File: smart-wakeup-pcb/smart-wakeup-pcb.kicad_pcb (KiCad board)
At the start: 2 copper layers, 42.5 x 29 mm, 21 parts, among them J1 Conn_01x03, J2 Conn_01x02, J3 Conn_01x04, J4 Conn_01x04, J5 Conn_01x02, J6 Conn_01x02, Q1 BSS138, Q2 BSS138, U1 XIAO-ESP32-S3-SMD, U2 MAX98357A

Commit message: reroute
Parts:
- added C4: 0.1u, Capacitor_SMD:C_0603_1608Metric, F.Cu at (143.5, 80.8)
- added U3: TMP102xxDRL, Package_TO_SOT_SMD:SOT-563, F.Cu at (141.0, 81.0)
- R1, R2, R3, R4: value R -> 10k; footprint Capacitor_SMD:C_0603_1608Metric -> Resistor_SMD:R_0603_1608Metric
- moved C1 6.69 mm to (140.2, 93.8), turned to -90 degrees
- moved R5 5.51 mm to (135.0, 92.5), turned to 90 degrees
- moved C2 3.45 mm to (137.7, 92.8), turned to 180 degrees
- moved R6 3.22 mm to (135.0, 89.4), turned to 90 degrees
- moved U2 2.65 mm to (138.4, 89.8), turned to 0 degrees
- moved R2 0.20 mm to (143.5, 84.3)
- moved R1 0.15 mm to (147.0, 81.8)
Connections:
- U1 pad 10: /I2S_BCLK -> /I2C_SCL_3V3
- U1 pad 11: /I2S_DIN -> /SW_1_IN
- U1 pad 3: unconnected-(U1-PA10_A2_D2-Pad3) -> /I2S_LRCLK
- U1 pad 5: /I2C_SDA_3V3 -> /I2S_BCLK
- U1 pad 6: /I2C_SCL_3V3 -> /I2S_DIN
- U1 pad 7: /SW_1_IN -> unconnected-(U1-PB08_A6_D6_TX-Pad7)
- U1 pad 9: /I2S_LRCLK -> /I2C_SDA_3V3
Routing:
- net /SW_1_IN: track 0.00 -> 38.9 mm
- net /I2S_LRCLK: track 3.87 -> 26.5 mm
- net /I2S_BCLK: track 1.91 -> 20.8 mm
- net GND: track 0.00 -> 17.7 mm, vias 0 -> 39
- net +3.3V: track 47.9 -> 65.4 mm
- net +5V: track 85.9 -> 102.6 mm
- net /SW_2_IN: track 0.00 -> 16.3 mm
- net /I2S_DIN: track 6.36 -> 14.9 mm
- net /I2C_SDA_3V3: track 32.9 -> 24.9 mm
- net Net-(J2-Pin_2): track 4.09 -> 10.1 mm, vias 0 -> 1
- net Net-(J2-Pin_1): track 3.75 -> 9.51 mm, vias 0 -> 1
- net /I2C_SCL_3V3: track 33.1 -> 32.2 mm, vias 0 -> 2
- net Net-(U2-GAIN_SLOT): track 3.05 -> 3.81 mm
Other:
- board size 42.5 x 29 mm -> 42.5 x 31.2 mm

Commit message: drc, holes, lux sensor
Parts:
- added C5: 1u, Capacitor_SMD:C_0603_1608Metric, F.Cu at (136.3, 79.0)
- added H1: MountingHole, MountingHole:MountingHole_2.2mm_M2, F.Cu at (112.0, 102.2)
- added H2: MountingHole, MountingHole:MountingHole_2.2mm_M2, F.Cu at (131.3, 77.8)
- added U4: LTR-303ALS-01, OptoDevice:Lite-On_LTR-303ALS-01, F.Cu at (136.3, 81.1)
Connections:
- U1 pad 14: +5V -> unconnected-(U1-5V-Pad14)
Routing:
- net +5V: track 102.6 -> 55.4 mm
- net +3.3V: track 65.4 -> 75.7 mm
- net /I2C_SDA_3V3: track 24.9 -> 29.7 mm
- net GND: track 17.7 -> 21.6 mm, vias 39 -> 41
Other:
- board size 42.5 x 31.2 mm -> 46.2 x 33.2 mm

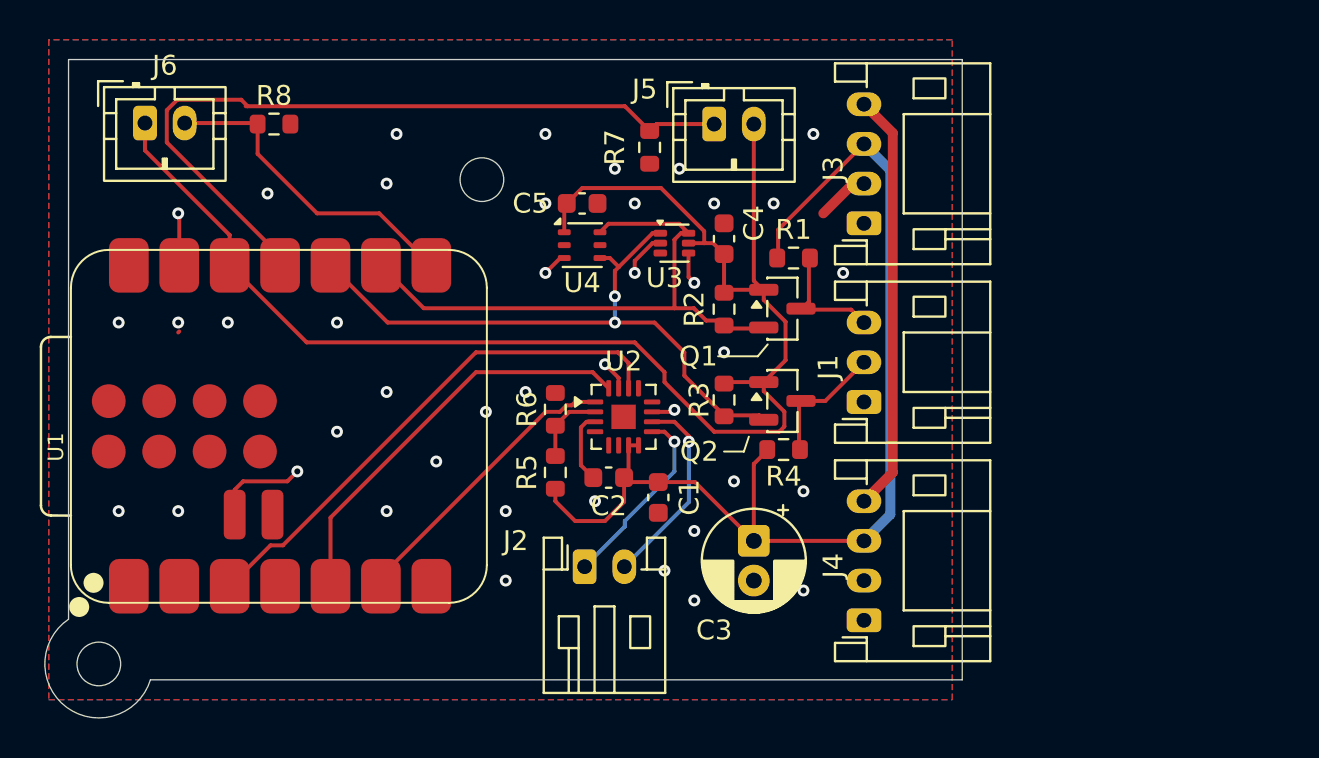
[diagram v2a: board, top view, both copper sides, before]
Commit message: labeling and test points
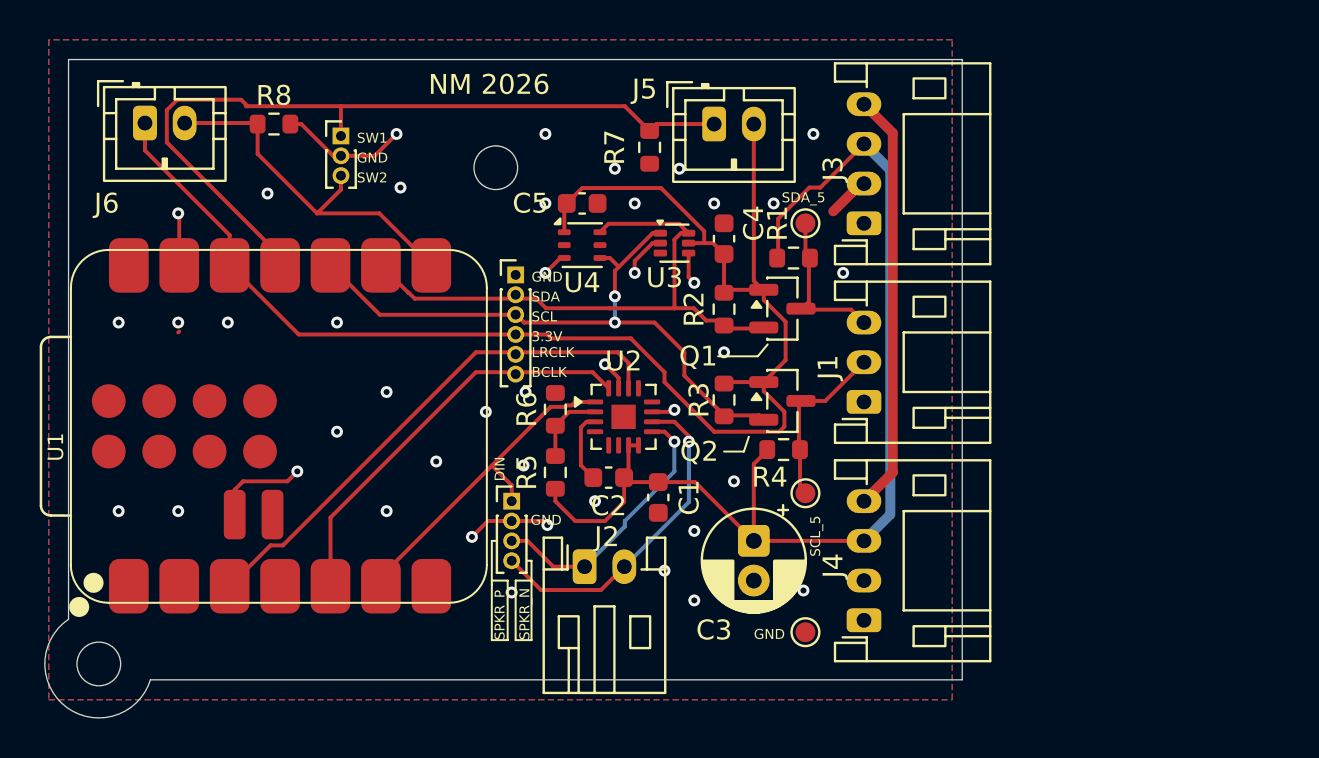
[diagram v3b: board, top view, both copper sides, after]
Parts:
- added J10: Conn_01x03, Connector_PinHeader_1.00mm:PinHeader_1x03_P1.00mm_Vertical, F.Cu at (124.2, 75.6)
- added J7: Conn_01x06, Connector_PinHeader_1.00mm:PinHeader_1x06_P1.00mm_Vertical, F.Cu at (133.0, 82.6)
- added J9: Conn_01x04, Connector_PinHeader_1.00mm:PinHeader_1x04_P1.00mm_Vertical, F.Cu at (132.8, 94.0)
- added TP1: TestPoint, TestPoint:TestPoint_Pad_D1.0mm, F.Cu at (147.6, 80.0)
- added TP2: TestPoint, TestPoint:TestPoint_Pad_D1.0mm, F.Cu at (147.6, 93.6)
- added TP3: TestPoint, TestPoint:TestPoint_Pad_D1.0mm, F.Cu at (147.6, 100.6)
- moved H2 0.92 mm to (132.0, 77.2)
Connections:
- net Net-(J2-Pin_1) renamed /SPKR_P
- net Net-(J2-Pin_2) renamed /SPKR_N
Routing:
- net GND: track 21.6 -> 32.3 mm, vias 41 -> 42
- net /SPKR_N: track 10.1 -> 16.8 mm
- net /SPKR_P: track 9.51 -> 13.7 mm
- net /SW_2_IN: track 16.3 -> 18.7 mm
- net /I2C_SCL: track 6.47 -> 8.79 mm
- net /I2S_DIN: track 14.9 -> 17.1 mm
- net /I2C_SDA: track 6.06 -> 7.90 mm
- net /SW_1_IN: track 38.9 -> 40.4 mm
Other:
- board text added: "3.3V"
- board text added: "BCLK"
- board text added: "DIN"
- board text added: "GND"
- board text added: "LRCLK"
- board text added: "NM 2026"
- board text added: "SCL"
- board text added: "SCL_5"
- board text added: "SDA"
- board text added: "SDA_5"
- board text added: "SPKR_N"
- board text added: "SPKR_P"
- board text added: "SW1"
- board text added: "SW2"
